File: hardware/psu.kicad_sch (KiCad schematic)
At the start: 48 parts, among them U401 XL1509, U402 XL1509

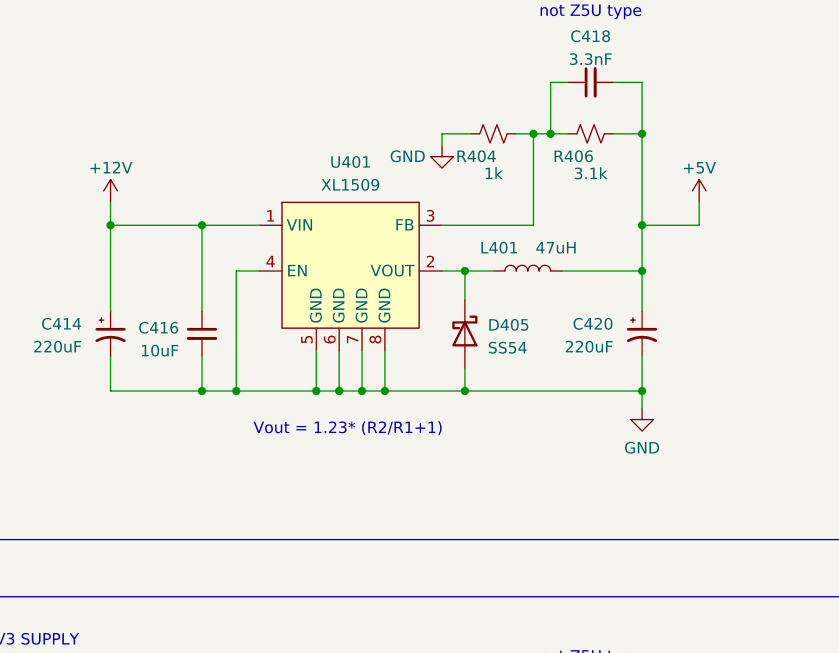
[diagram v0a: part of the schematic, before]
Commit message: work on firmware and swap solenoid banks to match actual pinout
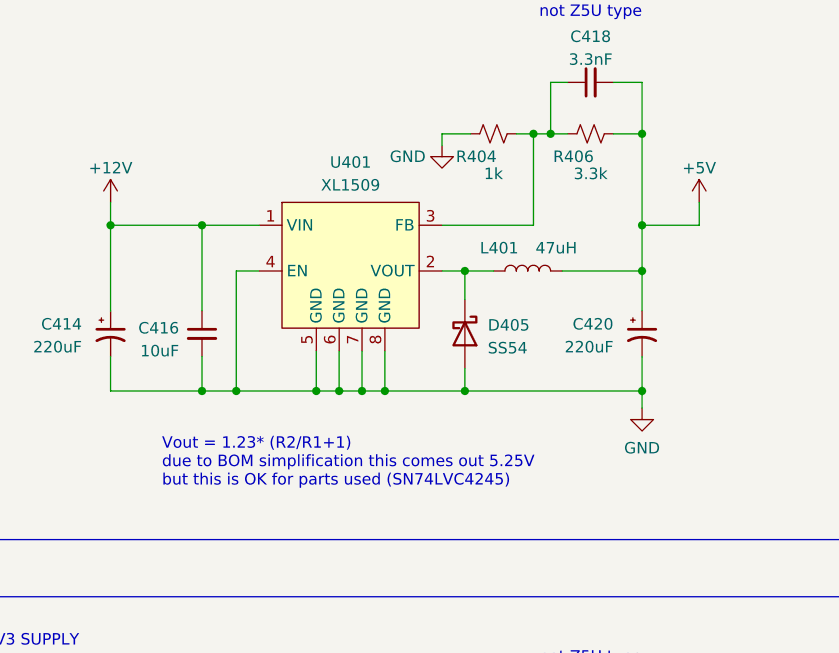
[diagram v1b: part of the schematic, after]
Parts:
- R406: value 3.1k -> 3.3k
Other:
- note added: "Vout = 1.23* (R2/R1+1) due to BOM simplification this comes out 5.25V but this is OK for parts used (SN74LVC4245)"
- note removed: "Vout = 1.23* (R2/R1+1)"
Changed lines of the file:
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@@
     (effects (font (size 1.27 1.27)) (justify left bottom))
   )
-  (text "Vout = 1.23* (R2/R1+1)" (at 213.36 74.93 0)
+  (text "Vout = 1.23* (R2/R1+1)\ndue to BOM simplification this comes out 5.25V \nbut this is OK for parts used (SN74LVC4245)"
+    (at 203.2 80.645 0)
     (effects (font (size 1.27 1.27)) (justify left bottom))
   )
@@
       (effects (font (size 1.27 1.27)))
     )
-    (property "Value" "3.1k" (at 250.825 45.72 90)
-      (effects (font (size 1.27 1.27)))
-    )
+    (property "Value" "3.3k" (at 250.825 45.72 90)
+      (effects (font (size 1.27 1.27)))
+    )
